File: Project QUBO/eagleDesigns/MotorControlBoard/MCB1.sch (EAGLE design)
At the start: 71 parts, among them U1 PCA9685

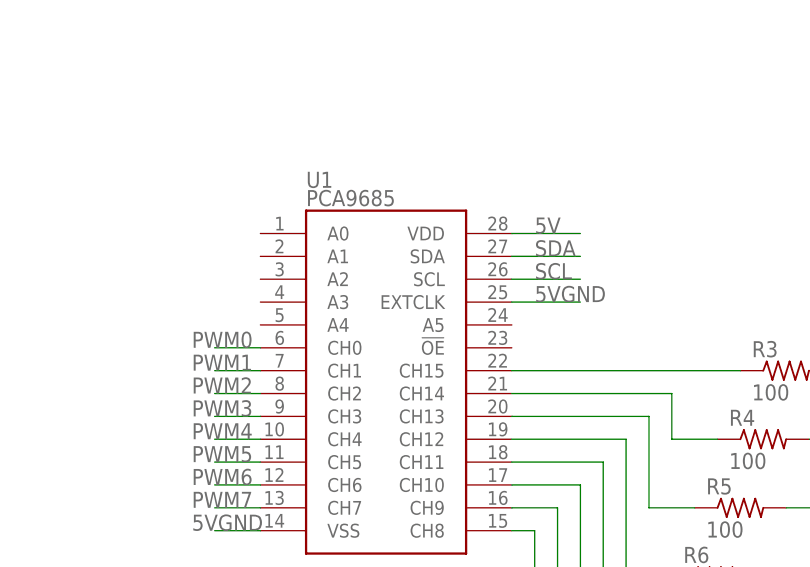
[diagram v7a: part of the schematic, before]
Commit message: finalize MCB
Devices still need to have packages designed. Pneumatics board still
needs to be integrated
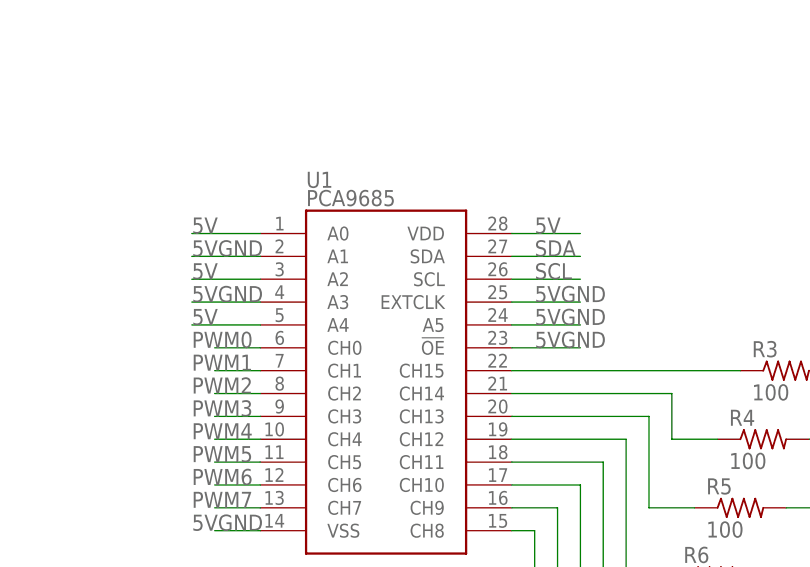
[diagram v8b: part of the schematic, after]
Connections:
- net 5V: now also U1.A0, U1.A2, U1.A4
- net 5VGND: now also U1.!OE, U1.A1, U1.A3, U1.A5
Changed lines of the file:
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@@
 <label x="167.64" y="58.42" size="1.778" layer="95"/>
+</segment>
+<segment>
+<pinref part="U1" gate="G$1" pin="A0"/>
+<wire x1="-101.6" y1="190.5" x2="-109.22" y2="190.5" width="0.1524" layer="91"/>
+<label x="-109.22" y="190.5" size="1.778" layer="95"/>
+</segment>
+<segment>
+<pinref part="U1" gate="G$1" pin="A2"/>
+<wire x1="-101.6" y1="185.42" x2="-109.22" y2="185.42" width="0.1524" layer="91"/>
+<label x="-109.22" y="185.42" size="1.778" layer="95"/>
+</segment>
+<segment>
+<pinref part="U1" gate="G$1" pin="A4"/>
+<wire x1="-101.6" y1="180.34" x2="-109.22" y2="180.34" width="0.1524" layer="91"/>
+<label x="-109.22" y="180.34" size="1.778" layer="95"/>
 </segment>
 </net>
@@
 <segment>
 <pinref part="U1" gate="G$1" pin="EXTCLK"/>
+<label x="-71.12" y="182.88" size="1.778" layer="95"/>
 <wire x1="-73.66" y1="182.88" x2="-66.04" y2="182.88" width="0.1524" layer="91"/>
-<label x="-71.12" y="182.88" size="1.778" layer="95"/>
 </segment>
 <segment>
@@
 <label x="-17.78" y="175.26" size="1.778" layer="95"/>
 </segment>
+<segment>
+<pinref part="U1" gate="G$1" pin="A1"/>
+<wire x1="-101.6" y1="187.96" x2="-109.22" y2="187.96" width="0.1524" layer="91"/>
+<label x="-109.22" y="187.96" size="1.778" layer="95"/>
+</segment>
+<segment>
+<pinref part="U1" gate="G$1" pin="A3"/>
+<wire x1="-101.6" y1="182.88" x2="-109.22" y2="182.88" width="0.1524" layer="91"/>
+<label x="-109.22" y="182.88" size="1.778" layer="95"/>
+</segment>
+<segment>
+<pinref part="U1" gate="G$1" pin="A5"/>
+<wire x1="-73.66" y1="180.34" x2="-66.04" y2="180.34" width="0.1524" layer="91"/>
+<label x="-71.12" y="180.34" size="1.778" layer="95"/>
+</segment>
+<segment>
+<pinref part="U1" gate="G$1" pin="!OE"/>
+<wire x1="-73.66" y1="177.8" x2="-66.04" y2="177.8" width="0.1524" layer="91"/>
+<label x="-71.12" y="177.8" size="1.778" layer="95"/>
+</segment>
 </net>
